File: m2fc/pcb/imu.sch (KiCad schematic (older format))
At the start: 50 parts, among them IC401 L3G4200D, IC402 ADXL375, IC403 HMC5883L, IC404 ADXL345, IC405 MS5611-01BA03

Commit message: add esd diodes to m2fc
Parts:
- C303: renamed from C405; footprint 1411 -> m2fc:C0603; Farnell 2333026 -> 1657936
- C306: renamed from C411; footprint 1411 -> m2fc:C0603; Farnell 2333026 -> 1657936
- C309: renamed from C401; footprint 1411 -> m2fc:C0603; Farnell 2333026 -> 1657936
- renumbered C403 to C301, C404 to C302, C409 to C304, C410 to C305, C414 to C307, C408 to C308, C402 to C310, C406 to C311, C412 to C312, C407 to C313, C413 to C314, IC402 to IC301, IC404 to IC302, IC405 to IC303, IC403 to IC304, IC401 to IC305, R403 to R301, R407 to R302, R401 to R303, R405 to R304, R402 to R305, R406 to R306, R408 to R307, R404 to R308, TP409 to TP301, TP414 to TP302, TP410 to TP303, TP415 to TP304, TP405 to TP305, TP416 to TP306, TP406 to TP307, TP417 to TP308, TP407 to TP309, TP418 to TP310, TP408 to TP311, TP419 to TP312, TP401 to TP313, TP411 to TP314, TP402 to TP315, TP412 to TP316, TP420 to TP317, TP421 to TP318, TP422 to TP319, TP413 to TP320, TP423 to TP321, TP403 to TP322, TP404 to TP323

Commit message: m2fc footprints, start layout
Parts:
- removed C303, C306, C309: 10µ, m2fc:C0603, symbol CP1
- removed C314: 4µ7, m2fc:C0603, symbol CP1
- added C303, C306, C309: 10µ, m2fc:C0603, symbol C
- added C314: 4µ7, m2fc:C0603, symbol C
- IC301, IC302: footprint (none) -> m2fc:ADXL3x5
- IC303: footprint (none) -> m2fc:MS5611-01BA
- IC304: footprint (none) -> m2fc:HMC5883L
- IC305: footprint (none) -> m2fc:L3G4200D

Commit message: routing continues
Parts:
- removed TP322, TP323: TESTPAD, m2fc:TESTPAD, symbol TESTPAD
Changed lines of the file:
@@
-	0    -1   -1   0
-$EndComp
-$Comp
-L TESTPAD TP322
-U 1 1 53B7FC94
-P 3950 4450
-F 0 "TP322" H 3980 4410 30  0000 C CNN
-F 1 "TESTPAD" H 3950 4500 60  0001 C CNN
-F 2 "m2fc:TESTPAD" H 3950 4450 60  0001 C CNN
-F 3 "" H 3950 4450 60  0000 C CNN
-	1    3950 4450
 	0    -1   -1   0
 $EndComp
 Connection ~ 3950 4050
 Connection ~ 3950 3950
-Connection ~ 3950 4450
 $Comp
 L TESTPAD TP314
@@
 Wire Wire Line
 	3800 4550 4000 4550
-$Comp
-L TESTPAD TP323
-U 1 1 53C45860
-P 3950 4550
-F 0 "TP323" H 3980 4510 30  0000 C CNN
-F 1 "TESTPAD" H 3950 4600 60  0001 C CNN
-F 2 "m2fc:TESTPAD" H 3950 4550 60  0001 C CNN
-F 3 "" H 3950 4550 60  0000 C CNN
-	1    3950 4550
-	0    -1   -1   0
-$EndComp
-Connection ~ 3950 4550
 Wire Wire Line
 	3800 4150 3850 4150

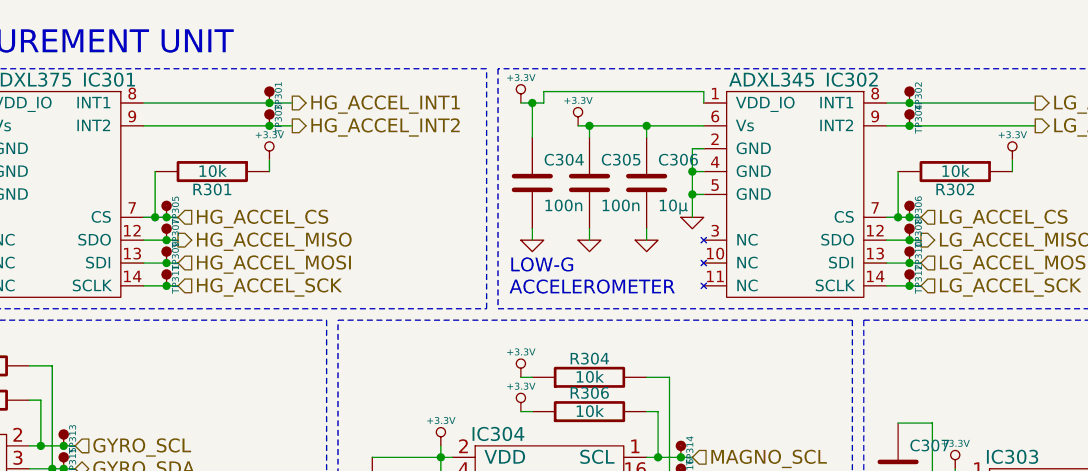
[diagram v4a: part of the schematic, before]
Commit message: routing intensifies
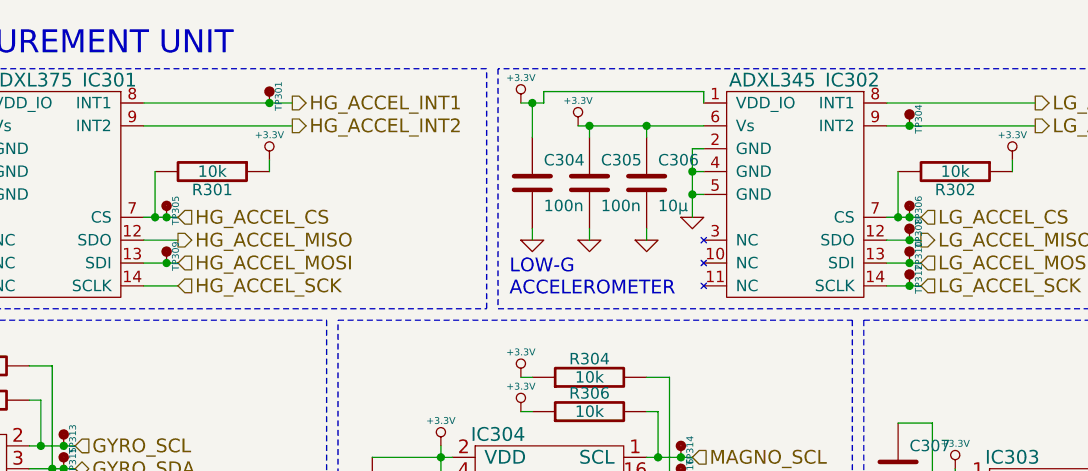
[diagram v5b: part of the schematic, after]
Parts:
- removed TP302, TP303, TP307, TP311: TESTPAD, m2fc:TESTPAD, symbol TESTPAD
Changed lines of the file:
@@
 $EndDescr
 $Comp
-L GND #PWR0106
+L GND #PWR311
 U 1 1 53B66CF6
 P 3250 3050
-F 0 "#PWR0106" H 3250 3050 30  0001 C CNN
+F 0 "#PWR311" H 3250 3050 30  0001 C CNN
 F 1 "GND" H 3250 2980 30  0001 C CNN
 F 2 "" H 3250 3050 60  0001 C CNN
@@
 HIGH-G\nACCELEROMETER
 $Comp
-L GND #PWR0107
+L GND #PWR307
 U 1 1 53B66D11
 P 3450 2950
-F 0 "#PWR0107" H 3450 2950 30  0001 C CNN
+F 0 "#PWR307" H 3450 2950 30  0001 C CNN
 F 1 "GND" H 3450 2880 30  0001 C CNN
 F 2 "" H 3450 2950 60  0001 C CNN
@@
 $EndComp
 $Comp
-L GND #PWR0108
+L GND #PWR309
 U 1 1 53B66D17
 P 2750 3050
-F 0 "#PWR0108" H 2750 3050 30  0001 C CNN
+F 0 "#PWR309" H 2750 3050 30  0001 C CNN
 F 1 "GND" H 2750 2980 30  0001 C CNN
 F 2 "" H 2750 3050 60  0001 C CNN
@@
 $EndComp
 $Comp
-L GND #PWR0109
+L GND #PWR310
 U 1 1 53B66D1D
 P 3000 3050
-F 0 "#PWR0109" H 3000 3050 30  0001 C CNN
+F 0 "#PWR310" H 3000 3050 30  0001 C CNN
 F 1 "GND" H 3000 2980 30  0001 C CNN
 F 2 "" H 3000 3050 60  0001 C CNN
@@
 $EndComp
 $Comp
-L GND #PWR0110
+L GND #PWR314
 U 1 1 53B66D3D
 P 6500 3050
-F 0 "#PWR0110" H 6500 3050 30  0001 C CNN
+F 0 "#PWR314" H 6500 3050 30  0001 C CNN
 F 1 "GND" H 6500 2980 30  0001 C CNN
 F 2 "" H 6500 3050 60  0001 C CNN
@@
 LOW-G\nACCELEROMETER
 $Comp
-L GND #PWR0111
+L GND #PWR308
 U 1 1 53B66D58
 P 6700 2950
-F 0 "#PWR0111" H 6700 2950 30  0001 C CNN
+F 0 "#PWR308" H 6700 2950 30  0001 C CNN
 F 1 "GND" H 6700 2880 30  0001 C CNN
 F 2 "" H 6700 2950 60  0001 C CNN
@@
 $EndComp
 $Comp
-L GND #PWR0112
+L GND #PWR312
 U 1 1 53B66D5E
 P 6000 3050
-F 0 "#PWR0112" H 6000 3050 30  0001 C CNN
+F 0 "#PWR312" H 6000 3050 30  0001 C CNN
 F 1 "GND" H 6000 2980 30  0001 C CNN
 F 2 "" H 6000 3050 60  0001 C CNN
@@
 $EndComp
 $Comp
-L GND #PWR0113
+L GND #PWR313
 U 1 1 53B66D64
 P 6250 3050
-F 0 "#PWR0113" H 6250 3050 30  0001 C CNN
+F 0 "#PWR313" H 6250 3050 30  0001 C CNN
 F 1 "GND" H 6250 2980 30  0001 C CNN
 F 2 "" H 6250 3050 60  0001 C CNN
@@
 $EndComp
 $Comp
-L +3.3V #PWR0114
+L +3.3V #PWR301
 U 1 1 53B66D83
 P 2700 2450
-F 0 "#PWR0114" H 2700 2410 30  0001 C CNN
+F 0 "#PWR301" H 2700 2410 30  0001 C CNN
 F 1 "+3.3V" H 2700 2560 30  0000 C CNN
 F 2 "" H 2700 2450 60  0000 C CNN
@@
 $EndComp
 $Comp
-L +3.3V #PWR0115
+L +3.3V #PWR303
 U 1 1 53B66D89
 P 2950 2550
-F 0 "#PWR0115" H 2950 2510 30  0001 C CNN
+F 0 "#PWR303" H 2950 2510 30  0001 C CNN
 F 1 "+3.3V" H 2950 2660 30  0000 C CNN
 F 2 "" H 2950 2550 60  0000 C CNN
@@
 $EndComp
 $Comp
-L +3.3V #PWR0116
+L +3.3V #PWR305
 U 1 1 53B66D8F
 P 4850 2700
-F 0 "#PWR0116" H 4850 2660 30  0001 C CNN
+F 0 "#PWR305" H 4850 2660 30  0001 C CNN
 F 1 "+3.3V" H 4850 2810 30  0000 C CNN
 F 2 "" H 4850 2700 60  0000 C CNN
@@
 $EndComp
 $Comp
-L +3.3V #PWR0117
+L +3.3V #PWR302
 U 1 1 53B66D95
 P 5950 2450
-F 0 "#PWR0117" H 5950 2410 30  0001 C CNN
+F 0 "#PWR302" H 5950 2410 30  0001 C CNN
 F 1 "+3.3V" H 5950 2560 30  0000 C CNN
 F 2 "" H 5950 2450 60  0000 C CNN
@@
 $EndComp
 $Comp
-L +3.3V #PWR0118
+L +3.3V #PWR304
 U 1 1 53B66D9B
 P 6200 2550
-F 0 "#PWR0118" H 6200 2510 30  0001 C CNN
+F 0 "#PWR304" H 6200 2510 30  0001 C CNN
 F 1 "+3.3V" H 6200 2660 30  0000 C CNN
 F 2 "" H 6200 2550 60  0000 C CNN
@@
 $EndComp
 $Comp
-L +3.3V #PWR0119
+L +3.3V #PWR306
 U 1 1 53B66DA1
 P 8100 2700
-F 0 "#PWR0119" H 8100 2660 30  0001 C CNN
+F 0 "#PWR306" H 8100 2660 30  0001 C CNN
 F 1 "+3.3V" H 8100 2810 30  0000 C CNN
 F 2 "" H 8100 2700 60  0000 C CNN
@@
 	4350 2750 4350 2950
 Wire Wire Line
-	4450 3250 4300 3250
-Wire Wire Line
 	4450 3050 4300 3050
 Connection ~ 3450 2750
@@
 	7550 2550 8200 2550
 $Comp
-L GND #PWR0120
+L GND #PWR326
 U 1 1 53B67965
 P 2900 4800
-F 0 "#PWR0120" H 2900 4800 30  0001 C CNN
+F 0 "#PWR326" H 2900 4800 30  0001 C CNN
 F 1 "GND" H 2900 4730 30  0001 C CNN
 F 2 "" H 2900 4800 60  0001 C CNN
@@
 $EndComp
 $Comp
-L GND #PWR0121
+L GND #PWR327
 U 1 1 53B679A7
 P 4950 5000
-F 0 "#PWR0121" H 4950 5000 30  0001 C CNN
+F 0 "#PWR327" H 4950 5000 30  0001 C CNN
 F 1 "GND" H 4950 4930 30  0001 C CNN
 F 2 "" H 4950 5000 60  0001 C CNN
@@
 GYROSCOPE
 $Comp
-L +3.3V #PWR0122
+L +3.3V #PWR315
 U 1 1 53B679AF
 P 3200 3600
-F 0 "#PWR0122" H 3200 3560 30  0001 C CNN
+F 0 "#PWR315" H 3200 3560 30  0001 C CNN
 F 1 "+3.3V" H 3200 3710 30  0000 C CNN
 F 2 "" H 3200 3600 60  0000 C CNN
@@
 $EndComp
 $Comp
-L +3.3V #PWR0123
+L +3.3V #PWR317
 U 1 1 53B679B5
 P 3200 3750
-F 0 "#PWR0123" H 3200 3710 30  0001 C CNN
+F 0 "#PWR317" H 3200 3710 30  0001 C CNN
 F 1 "+3.3V" H 3200 3860 30  0000 C CNN
 F 2 "" H 3200 3750 60  0000 C CNN
@@
 $EndComp
 $Comp
-L +3.3V #PWR0124
+L +3.3V #PWR322
 U 1 1 53B679BB
 P 3950 4250
-F 0 "#PWR0124" H 3950 4210 30  0001 C CNN
+F 0 "#PWR322" H 3950 4210 30  0001 C CNN
 F 1 "+3.3V" H 3950 4360 30  0000 C CNN
 F 2 "" H 3950 4250 60  0000 C CNN
@@
 $EndComp
 $Comp
-L +3.3V #PWR0125
+L +3.3V #PWR319
 U 1 1 53B679C1
 P 2900 3900
-F 0 "#PWR0125" H 2900 3860 30  0001 C CNN
+F 0 "#PWR319" H 2900 3860 30  0001 C CNN
 F 1 "+3.3V" H 2900 4010 30  0000 C CNN
 F 2 "" H 2900 3900 60  0000 C CNN
@@
 $EndComp
 $Comp
-L GND #PWR0126
+L GND #PWR328
 U 1 1 53B67FC7
 P 7100 5050
-F 0 "#PWR0126" H 7100 5050 30  0001 C CNN
+F 0 "#PWR328" H 7100 5050 30  0001 C CNN
 F 1 "GND" H 7100 4980 30  0001 C CNN
 F 2 "" H 7100 5050 60  0001 C CNN
@@
 $EndComp
 $Comp
-L GND #PWR0127
+L GND #PWR324
 U 1 1 53B67FD5
 P 5600 4450
-F 0 "#PWR0127" H 5600 4450 30  0001 C CNN
+F 0 "#PWR324" H 5600 4450 30  0001 C CNN
 F 1 "GND" H 5600 4380 30  0001 C CNN
 F 2 "" H 5600 4450 60  0001 C CNN
@@
 MAGNETOMETER
 $Comp
-L +3.3V #PWR0128
+L +3.3V #PWR316
 U 1 1 53B67FE4
 P 5950 3650
-F 0 "#PWR0128" H 5950 3610 30  0001 C CNN
+F 0 "#PWR316" H 5950 3610 30  0001 C CNN
 F 1 "+3.3V" H 5950 3760 30  0000 C CNN
 F 2 "" H 5950 3650 60  0000 C CNN
@@
 $EndComp
 $Comp
-L +3.3V #PWR0129
+L +3.3V #PWR318
 U 1 1 53B67FEA
 P 5950 3800
-F 0 "#PWR0129" H 5950 3760 30  0001 C CNN
+F 0 "#PWR318" H 5950 3760 30  0001 C CNN
 F 1 "+3.3V" H 5950 3910 30  0000 C CNN
 F 2 "" H 5950 3800 60  0000 C CNN
@@
 $EndComp
 $Comp
-L +3.3V #PWR0130
+L +3.3V #PWR320
 U 1 1 53B67FF0
 P 5600 3950
-F 0 "#PWR0130" H 5600 3910 30  0001 C CNN
+F 0 "#PWR320" H 5600 3910 30  0001 C CNN
 F 1 "+3.3V" H 5600 4060 30  0000 C CNN
 F 2 "" H 5600 3950 60  0000 C CNN
@@
 BAROMETER
 $Comp
-L GND #PWR0131
+L GND #PWR323
 U 1 1 53B686F3
 P 7800 4350
-F 0 "#PWR0131" H 7800 4350 30  0001 C CNN
+F 0 "#PWR323" H 7800 4350 30  0001 C CNN
 F 1 "GND" H 7800 4280 30  0001 C CNN
 F 2 "" H 7800 4350 60  0001 C CNN
@@
 $EndComp
 $Comp
-L +3.3V #PWR0132
+L +3.3V #PWR321
 U 1 1 53B6870C
 P 7850 4050
-F 0 "#PWR0132" H 7850 4010 30  0001 C CNN
+F 0 "#PWR321" H 7850 4010 30  0001 C CNN
 F 1 "+3.3V" H 7850 4160 30  0000 C CNN
 F 2 "" H 7850 4050 60  0000 C CNN
@@
 $EndComp
 $Comp
-L +3.3V #PWR0133
+L +3.3V #PWR325
 U 1 1 53B68712
 P 9300 4500
-F 0 "#PWR0133" H 9300 4460 30  0001 C CNN
+F 0 "#PWR325" H 9300 4460 30  0001 C CNN
 F 1 "+3.3V" H 9300 4610 30  0000 C CNN
 F 2 "" H 9300 4500 60  0000 C CNN
@@
 $EndComp
 $Comp
-L TESTPAD TP303
-U 1 1 53B7EA40
-P 4850 2550
-F 0 "TP303" H 4880 2510 30  0000 C CNN
-F 1 "TESTPAD" H 4850 2600 60  0001 C CNN
-F 2 "m2fc:TESTPAD" H 4850 2550 60  0001 C CNN
-F 3 "" H 4850 2550 60  0000 C CNN
-	1    4850 2550
-	0    -1   -1   0
-$EndComp
-$Comp
 L TESTPAD TP305
 U 1 1 53B7EA8E
@@
 	0    -1   -1   0
 $EndComp
-$Comp
-L TESTPAD TP307
-U 1 1 53B7EB4A
-P 4400 3050
-F 0 "TP307" H 4430 3010 30  0000 C CNN
-F 1 "TESTPAD" H 4400 3100 60  0001 C CNN
-F 2 "m2fc:TESTPAD" H 4400 3050 60  0001 C CNN
-F 3 "" H 4400 3050 60  0000 C CNN
-	1    4400 3050
-	0    -1   -1   0
-$EndComp
-$Comp
-L TESTPAD TP309
-U 1 1 53B7EB7D
-P 4400 3150
-F 0 "TP309" H 4430 3110 30  0000 C CNN
-F 1 "TESTPAD" H 4400 3200 60  0001 C CNN
-F 2 "m2fc:TESTPAD" H 4400 3150 60  0001 C CNN
-F 3 "" H 4400 3150 60  0000 C CNN
-	1    4400 3150
-	0    -1   -1   0
-$EndComp
-$Comp
-L TESTPAD TP311
-U 1 1 53B7EBB1
-P 4400 3250
-F 0 "TP311" H 4430 3210 30  0000 C CNN
-F 1 "TESTPAD" H 4400 3300 60  0001 C CNN
-F 2 "m2fc:TESTPAD" H 4400 3250 60  0001 C CNN
-F 3 "" H 4400 3250 60  0000 C CNN
-	1    4400 3250
-	0    -1   -1   0
-$EndComp
 Connection ~ 4850 2450
-Connection ~ 4850 2550
 Connection ~ 4400 2950
-Connection ~ 4400 3050
-Connection ~ 4400 3150
-Connection ~ 4400 3250
-$Comp
-L TESTPAD TP302
-U 1 1 53B7EBF2
-P 7650 2450
-F 0 "TP302" H 7680 2410 30  0000 C CNN
-F 1 "TESTPAD" H 7650 2500 60  0001 C CNN
-F 2 "m2fc:TESTPAD" H 7650 2450 60  0001 C CNN
-F 3 "" H 7650 2450 60  0000 C CNN
-	1    7650 2450
-	0    -1   -1   0
-$EndComp
 $Comp
 L TESTPAD TP304
@@
 Connection ~ 7650 2950
 Connection ~ 7650 2550
-Connection ~ 7650 2450
 $Comp
 L TESTPAD TP317
@@
 	0    1    1    0
 $EndComp
+Connection ~ 4400 3150
+$Comp
+L TESTPAD TP309
+U 1 1 53B7EB7D
+P 4400 3150
+F 0 "TP309" H 4430 3110 30  0000 C CNN
+F 1 "TESTPAD" H 4400 3200 60  0001 C CNN
+F 2 "m2fc:TESTPAD" H 4400 3150 60  0001 C CNN
+F 3 "" H 4400 3150 60  0000 C CNN
+	1    4400 3150
+	0    -1   -1   0
+$EndComp
+Wire Wire Line
+	4450 3250 4300 3250
 $EndSCHEMATC

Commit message: rescue symbols from m2fc pcb
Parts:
- C301, C302, C303, C304, C305, C306, C307, C308, C309, C310, C311, C312, C313, C314: symbol C -> C-RESCUE-m2fc
- R301, R302, R303, R304, R305, R306, R307, R308: symbol R -> R-RESCUE-m2fc
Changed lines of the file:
@@
 EESchema Schematic File Version 2
+LIBS:m2fc-rescue
 LIBS:power
 LIBS:device
@@
 LIBS:memory
 LIBS:xilinx
-LIBS:special
 LIBS:microcontrollers
 LIBS:dsp
@@
 LIBS:cga0402mlc-12g
 LIBS:m2fc-cache
-EELAYER 24 0
+EELAYER 25 0
 EELAYER END
 $Descr A4 11693 8268
@@
 $EndDescr
 $Comp
-L GND #PWR0106
+L GND-RESCUE-m2fc #PWR0106
 U 1 1 53B66CF6
 P 3250 3050
@@
 $EndComp
 $Comp
-L R R301
+L R-RESCUE-m2fc R301
 U 1 1 53B66D05
 P 4600 2750
@@
 HIGH-G\nACCELEROMETER
 $Comp
-L GND #PWR0107
+L GND-RESCUE-m2fc #PWR0107
 U 1 1 53B66D11
 P 3450 2950
@@
 $EndComp
 $Comp
-L GND #PWR0108
+L GND-RESCUE-m2fc #PWR0108
 U 1 1 53B66D17
 P 2750 3050
@@
 $EndComp
 $Comp
-L GND #PWR0109
+L GND-RESCUE-m2fc #PWR0109
 U 1 1 53B66D1D
 P 3000 3050
@@
 $EndComp
 $Comp
-L C C301
+L C-RESCUE-m2fc C301
 U 1 1 53B66D24
 P 2750 2800
@@
 $EndComp
 $Comp
-L C C302
+L C-RESCUE-m2fc C302
 U 1 1 53B66D2C
 P 3000 2800
@@
 $EndComp
 $Comp
-L GND #PWR0110
+L GND-RESCUE-m2fc #PWR0110
 U 1 1 53B66D3D
 P 6500 3050
@@
 $EndComp
 $Comp
-L R R302
+L R-RESCUE-m2fc R302
 U 1 1 53B66D4C
 P 7850 2750
@@
 LOW-G\nACCELEROMETER
 $Comp
-L GND #PWR0111
+L GND-RESCUE-m2fc #PWR0111
 U 1 1 53B66D58
 P 6700 2950
@@
 $EndComp
 $Comp
-L GND #PWR0112
+L GND-RESCUE-m2fc #PWR0112
 U 1 1 53B66D5E
 P 6000 3050
@@
 $EndComp
 $Comp
-L GND #PWR0113
+L GND-RESCUE-m2fc #PWR0113
 U 1 1 53B66D64
 P 6250 3050
@@
 $EndComp
 $Comp
-L C C304
+L C-RESCUE-m2fc C304
 U 1 1 53B66D6B
 P 6000 2800
@@
 $EndComp
 $Comp
-L C C305
+L C-RESCUE-m2fc C305
 U 1 1 53B66D73
 P 6250 2800
@@
 $EndComp
 $Comp
-L +3.3V #PWR0114
+L +3.3V-RESCUE-m2fc #PWR0114
 U 1 1 53B66D83
 P 2700 2450
@@
 $EndComp
 $Comp
-L +3.3V #PWR0115
+L +3.3V-RESCUE-m2fc #PWR0115
 U 1 1 53B66D89
 P 2950 2550
@@
 $EndComp
 $Comp
-L +3.3V #PWR0116
+L +3.3V-RESCUE-m2fc #PWR0116
 U 1 1 53B66D8F
 P 4850 2700
@@
 $EndComp
 $Comp
-L +3.3V #PWR0117
+L +3.3V-RESCUE-m2fc #PWR0117
 U 1 1 53B66D95
 P 5950 2450
@@
 $EndComp
 $Comp
-L +3.3V #PWR0118
+L +3.3V-RESCUE-m2fc #PWR0118
 U 1 1 53B66D9B
 P 6200 2550
@@
 $EndComp
 $Comp
-L +3.3V #PWR0119
+L +3.3V-RESCUE-m2fc #PWR0119
 U 1 1 53B66DA1
 P 8100 2700
@@
 	7550 2550 8200 2550
 $Comp
-L GND #PWR0120
+L GND-RESCUE-m2fc #PWR0120
 U 1 1 53B67965
 P 2900 4800
@@
 $EndComp
 $Comp
-L R R305
+L R-RESCUE-m2fc R305
 U 1 1 53B6796C
 P 3550 3750
@@
 $EndComp
 $Comp
-L R R303
+L R-RESCUE-m2fc R303
 U 1 1 53B67974
 P 3550 3600
@@
 $EndComp
 $Comp
-L C C310
+L C-RESCUE-m2fc C310
 U 1 1 53B6797E
 P 2650 4300
@@
 $EndComp
 $Comp
-L R R308
+L R-RESCUE-m2fc R308
 U 1 1 53B67990
 P 4650 4950
@@
 $EndComp
 $Comp
-L C C311
+L C-RESCUE-m2fc C311
 U 1 1 53B67998
 P 4100 4750
@@
 $EndComp
 $Comp
-L C C313
+L C-RESCUE-m2fc C313
 U 1 1 53B679A0
 P 4100 4950
@@
 $EndComp
 $Comp
-L GND #PWR0121
+L GND-RESCUE-m2fc #PWR0121
 U 1 1 53B679A7
 P 4950 5000
@@
 GYROSCOPE
 $Comp
-L +3.3V #PWR0122
+L +3.3V-RESCUE-m2fc #PWR0122
 U 1 1 53B679AF
 P 3200 3600
@@
 $EndComp
 $Comp
-L +3.3V #PWR0123
+L +3.3V-RESCUE-m2fc #PWR0123
 U 1 1 53B679B5
 P 3200 3750
@@
 $EndComp
 $Comp
-L +3.3V #PWR0124
+L +3.3V-RESCUE-m2fc #PWR0124
 U 1 1 53B679BB
 P 3950 4250
@@
 $EndComp
 $Comp
-L +3.3V #PWR0125
+L +3.3V-RESCUE-m2fc #PWR0125
 U 1 1 53B679C1
 P 2900 3900
@@
 $EndComp
 $Comp
-L R R306
+L R-RESCUE-m2fc R306
 U 1 1 53B67FAF
 P 6250 3800
@@
 $EndComp
 $Comp
-L R R304
+L R-RESCUE-m2fc R304
 U 1 1 53B67FB7
 P 6250 3650
@@
 $EndComp
 $Comp
-L GND #PWR0126
+L GND-RESCUE-m2fc #PWR0126
 U 1 1 53B67FC7
 P 7100 5050
@@
 $EndComp
 $Comp
-L C C312
+L C-RESCUE-m2fc C312
 U 1 1 53B67FCE
 P 6800 4800
@@
 $EndComp
 $Comp
-L GND #PWR0127
+L GND-RESCUE-m2fc #PWR0127
 U 1 1 53B67FD5
 P 5600 4450
@@
 $EndComp
 $Comp
-L C C308
+L C-RESCUE-m2fc C308
 U 1 1 53B67FDC
 P 5300 4200
@@
 MAGNETOMETER
 $Comp
-L +3.3V #PWR0128
+L +3.3V-RESCUE-m2fc #PWR0128
 U 1 1 53B67FE4
 P 5950 3650
@@
 $EndComp
 $Comp
-L +3.3V #PWR0129
+L +3.3V-RESCUE-m2fc #PWR0129
 U 1 1 53B67FEA
 P 5950 3800
@@
 $EndComp
 $Comp
-L +3.3V #PWR0130
+L +3.3V-RESCUE-m2fc #PWR0130
 U 1 1 53B67FF0
 P 5600 3950
@@
 	5150 5250 5150 3400
 $Comp
-L R R307
+L R-RESCUE-m2fc R307
 U 1 1 53B686EA
 P 9000 4550
@@
 BAROMETER
 $Comp
-L GND #PWR0131
+L GND-RESCUE-m2fc #PWR0131
 U 1 1 53B686F3
 P 7800 4350
@@
 $EndComp
 $Comp
-L C C307
+L C-RESCUE-m2fc C307
 U 1 1 53B686FD
 P 7600 4050
@@
 $EndComp
 $Comp
-L +3.3V #PWR0132
+L +3.3V-RESCUE-m2fc #PWR0132
 U 1 1 53B6870C
 P 7850 4050
@@
 $EndComp
 $Comp
-L +3.3V #PWR0133
+L +3.3V-RESCUE-m2fc #PWR0133
 U 1 1 53B68712
 P 9300 4500
@@
 $EndComp
 $Comp
-L C C303
+L C-RESCUE-m2fc C303
 U 1 1 53D86DFD
 P 3250 2800
@@
 $EndComp
 $Comp
-L C C306
+L C-RESCUE-m2fc C306
 U 1 1 53D870F1
 P 6500 2800
@@
 $EndComp
 $Comp
-L C C309
+L C-RESCUE-m2fc C309
 U 1 1 53D87447
 P 2400 4300
@@
 $EndComp
 $Comp
-L C C314
+L C-RESCUE-m2fc C314
 U 1 1 53D90BCC
 P 6850 5000
